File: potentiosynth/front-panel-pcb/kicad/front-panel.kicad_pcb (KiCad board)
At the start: 2 copper layers, 127 x 50.8 mm, 38 parts, among them J1 Conn_01x40

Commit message: first draft front panel
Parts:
- added D10: LED, Diode_SMD:D_1206_3216Metric, F.Cu at (55.9, 128.3)
- added D9: LED, Diode_SMD:D_1206_3216Metric, F.Cu at (55.9, 113.0)
- added J_WRK1: Conn_01x01, Connector:Banana_Jack_1Pin, F.Cu at (69.8, 123.8)
- added J_WRK2: Conn_01x01, Connector:Banana_Jack_1Pin, F.Cu at (82.5, 123.8)
- added J_WRK3: Conn_01x01, Connector:Banana_Jack_1Pin, F.Cu at (95.2, 123.8)
- added J_WRK4: Conn_01x01, Connector:Banana_Jack_1Pin, F.Cu at (108.0, 123.8)
- added J_WRK5: Conn_01x01, Connector:Banana_Jack_1Pin, F.Cu at (120.7, 123.8)
- added J_WRK6: Conn_01x01, Connector:Banana_Jack_1Pin, F.Cu at (133.3, 123.8)
- added J_WRK7: Conn_01x01, Connector:Banana_Jack_1Pin, F.Cu at (146.1, 123.8)
- added J_WRK8: Conn_01x01, Connector:Banana_Jack_1Pin, F.Cu at (158.8, 123.8)
- added R10: 1k, Resistor_SMD:R_1206_3216Metric, B.Cu at (55.9, 128.3)
- added R9: 1k, Resistor_SMD:R_1206_3216Metric, B.Cu at (55.9, 113.0)
- added SW1: SW_SPDT, Connector_PinHeader_2.54mm:PinHeader_1x03_P2.54mm_Horizontal, F.Cu at (61.0, 123.2)
- renumbered J_ANO1 to J_COU1, J_ANO2 to J_COU2, J_ANO3 to J_COU3, J_ANO4 to J_COU4, J_ANO5 to J_COU5, J_ANO6 to J_COU6, J_ANO7 to J_COU7, J_ANO8 to J_COU8, J_CAT1 to J_REF1, J_CAT2 to J_REF2, J_CAT3 to J_REF3, J_CAT4 to J_REF4, J_CAT5 to J_REF5, J_CAT6 to J_REF6, J_CAT7 to J_REF7, J_CAT8 to J_REF8
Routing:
- net +15V: track 160.5 -> 213.6 mm
- net WORKING: track 0.00 -> 9.89 mm
- net Net-(D9-Pad2): track 0.00 -> 4.76 mm, vias 0 -> 1
- net Net-(D10-Pad2): track 0.00 -> 4.76 mm, vias 0 -> 1
- added copper zone on B.Cu, net +15V
- added copper zone on B.Cu, net WORKING
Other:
- board size 127 x 50.8 mm -> 127 x 70.5 mm
- board text added: "FRONT PANEL REVISION A MAY 2021"
- board text added: "OXIDATION"
- board text added: "POTENTIOSYNTH"
- board text added: "REDUCTION"
- board text removed: "FRONT PANEL REVISION 1.3.1 MARCH 2020"
- board text removed: "GALVANOSYNTH"

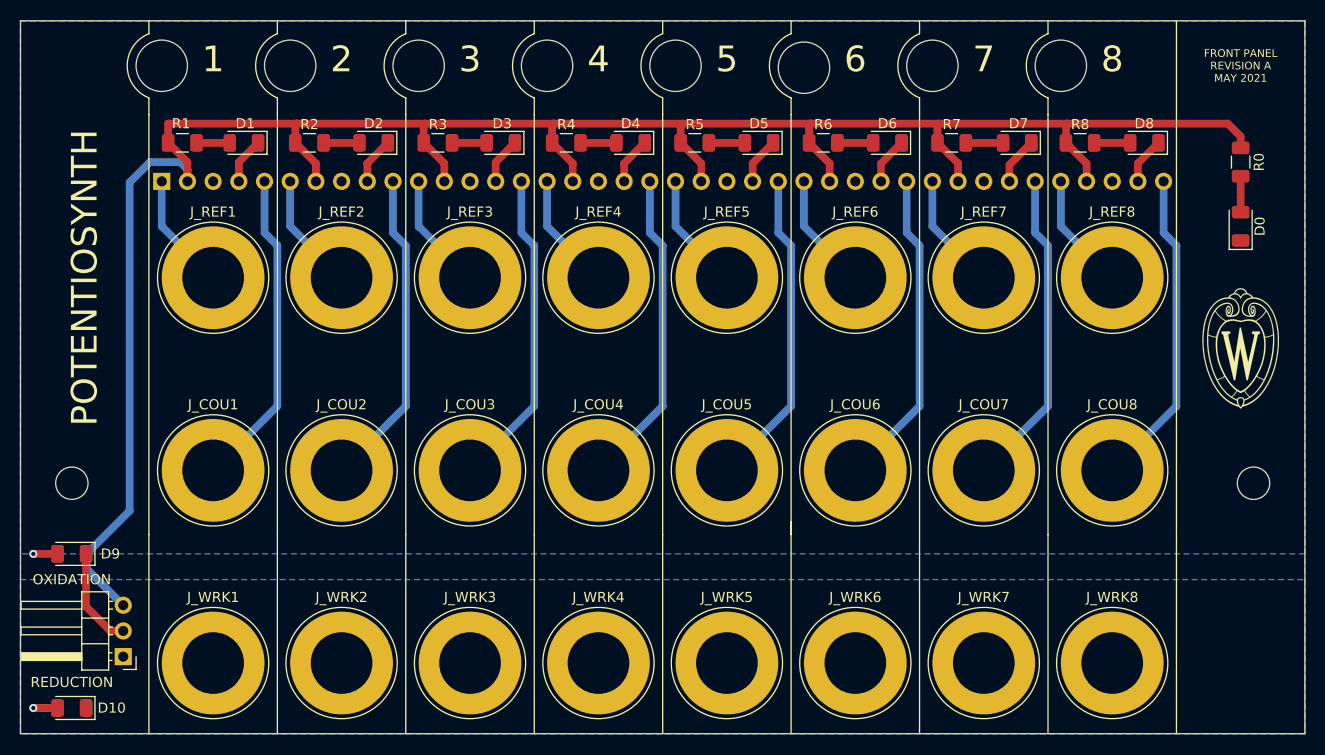
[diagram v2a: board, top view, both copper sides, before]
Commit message: fixed potentiosynth front panel silkscreen
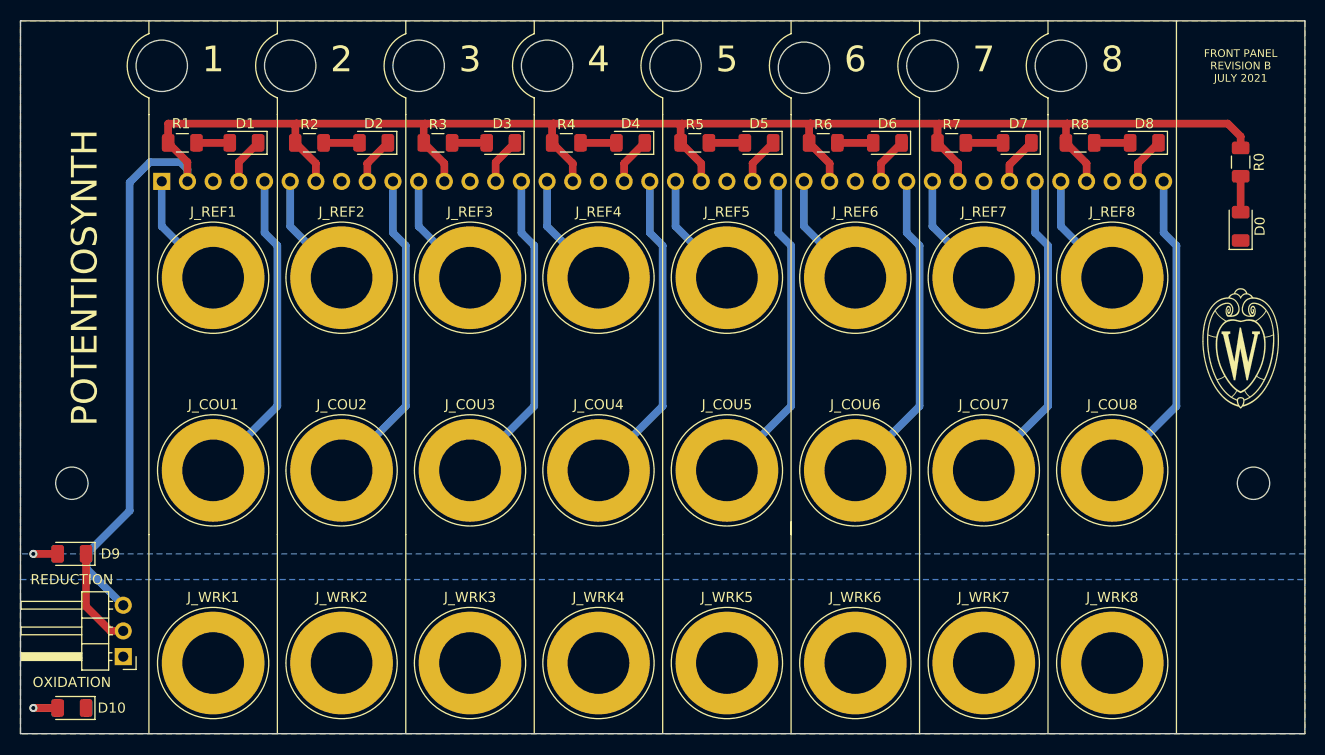
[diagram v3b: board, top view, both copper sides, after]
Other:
- board text added: "FRONT PANEL REVISION B JULY 2021"
- board text removed: "FRONT PANEL REVISION A MAY 2021"
